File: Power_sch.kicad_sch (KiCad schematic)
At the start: 13 parts, among them J1 USB4105-GF-A, J2 USB4105-GF-A, U1 LD39200PU33R, U2 TPD2EUSB30ADRTR

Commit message: Updata the USB Hub Sheet
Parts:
- R1: footprint (none) -> Resistor_SMD:R_0402_1005Metric
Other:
- note removed: "POWER_ESD"
- moved on the sheet: D3, D4, F1, J1, J2, R1, R2, R3, R4, U1, U2

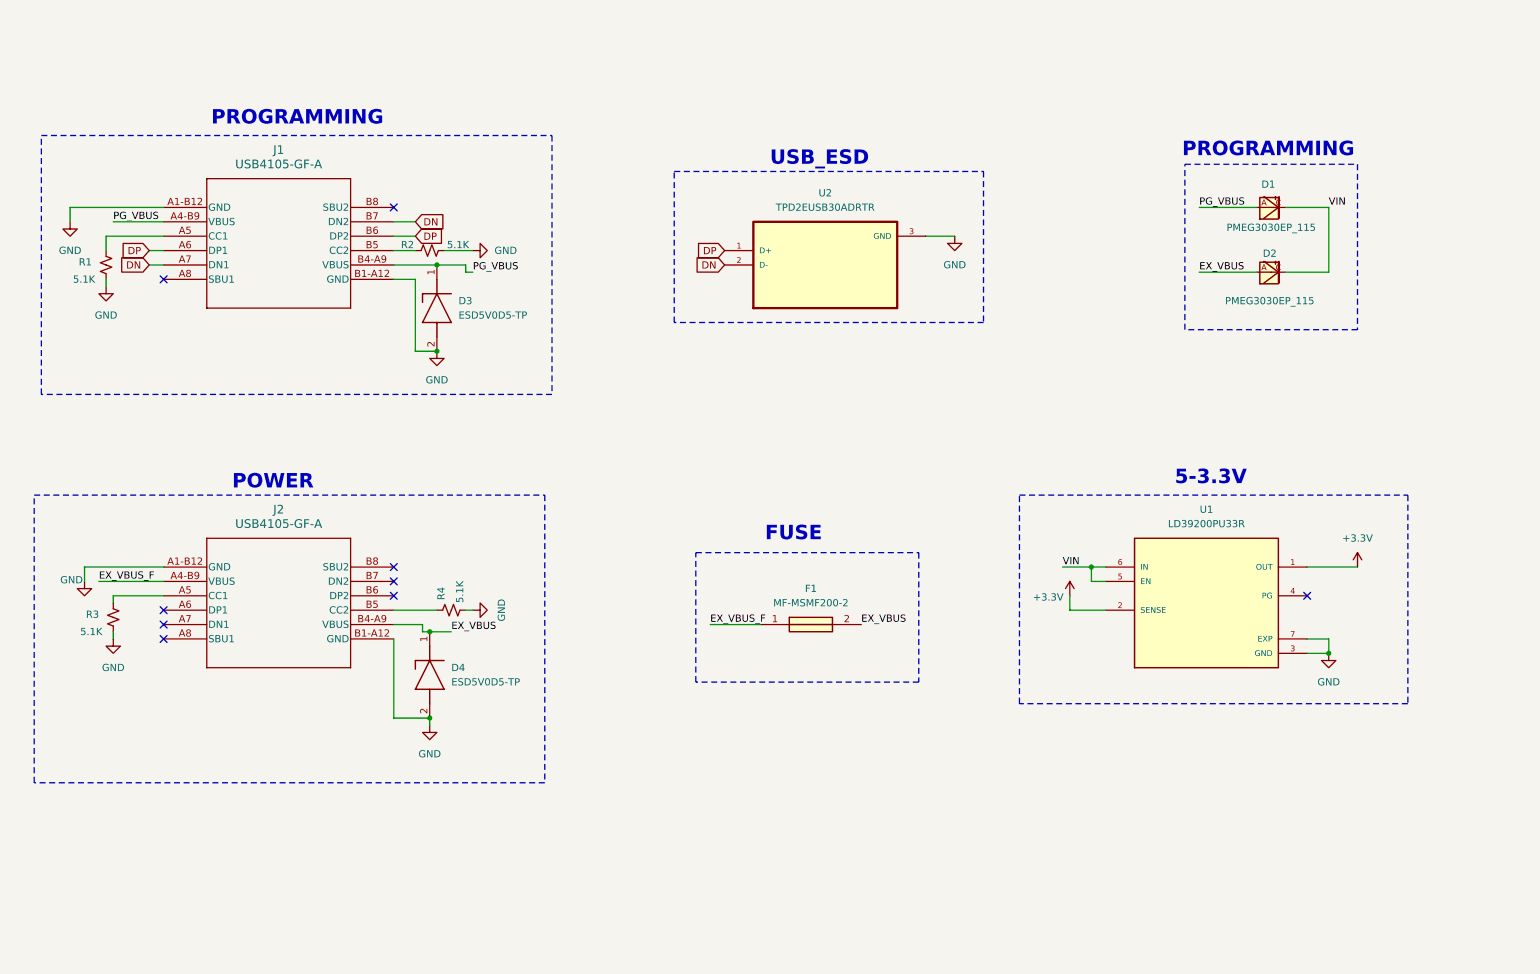
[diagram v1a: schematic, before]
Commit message: update the power sheet
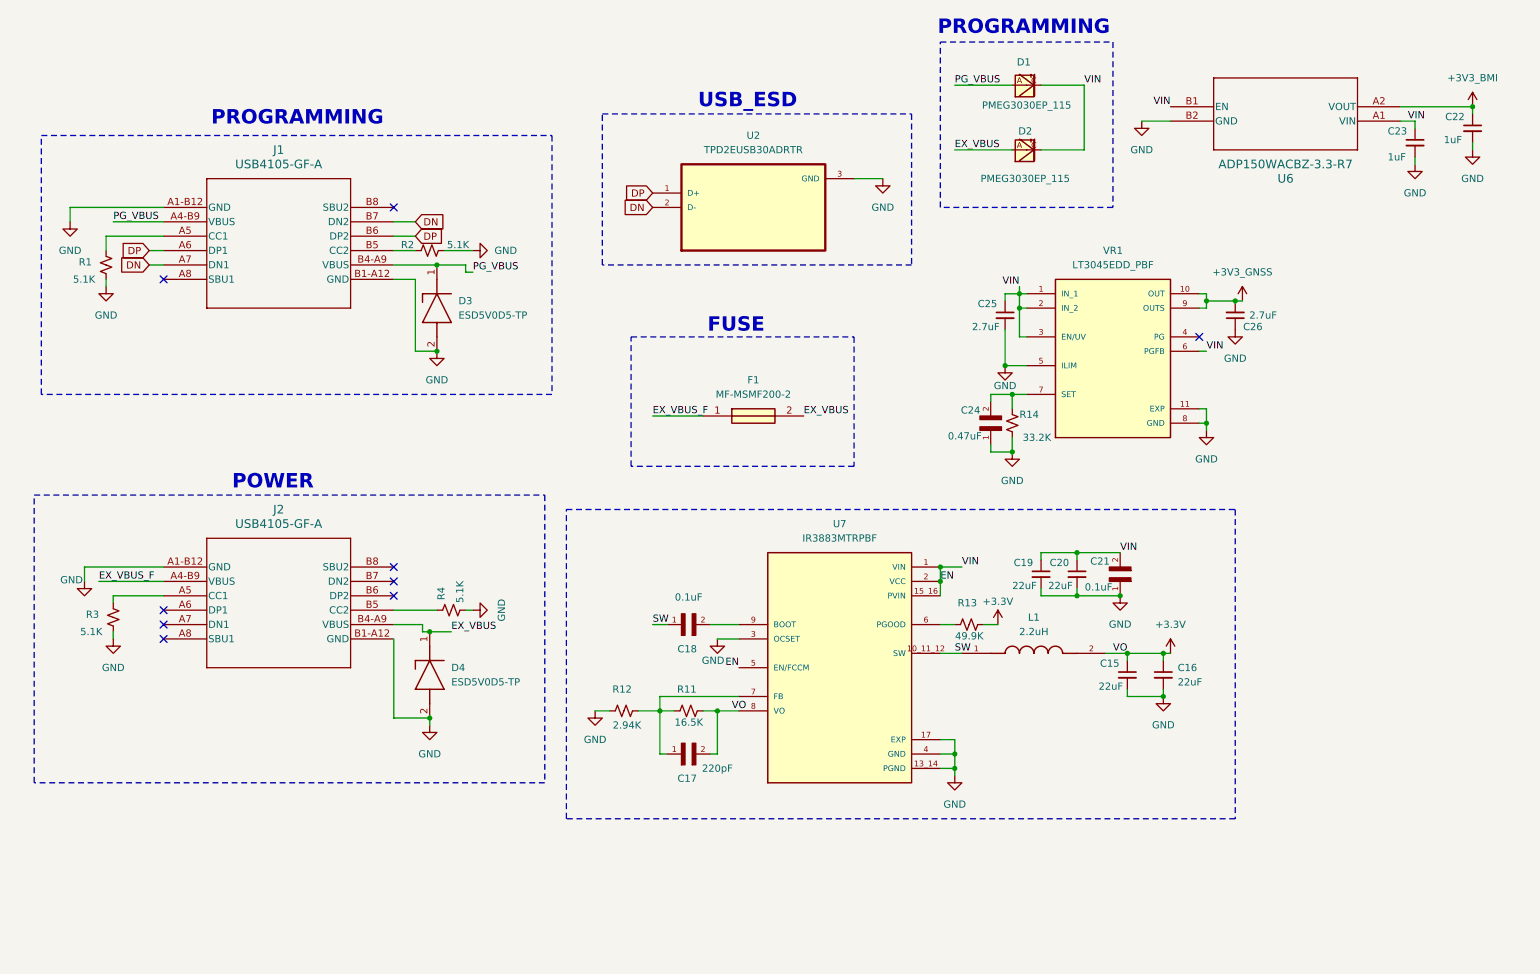
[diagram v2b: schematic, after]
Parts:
- removed U1: LD39200PU33R, LD39200PU33R:SON95P300X300X100-7N, symbol LD39200PU33R:LD39200PU33R
- added C15, C16, C19, C20: 22uF, Capacitor_SMD:C_0805_2012Metric, symbol Device:C_Small
- added C17: 220pF, C0402C104K4RAC:CAPC1005X55N, symbol C0402C104K4RAC:C0402C104K4RAC
- added C18, C21: 0.1uF, C0402C104K4RAC:CAPC1005X55N, symbol C0402C104K4RAC:C0402C104K4RAC
- added C22, C23: 1uF, Capacitor_SMD:C_0805_2012Metric, symbol Device:C_Small
- added C24: 0.47uF, C0402C104K4RAC:CAPC1005X55N, symbol C0402C104K4RAC:C0402C104K4RAC
- added C25, C26: 2.7uF, Capacitor_SMD:C_0805_2012Metric, symbol Device:C_Small
- added L1: 2.2uH, ASPIAIG-F5030-2R2M-T:IND_ASPIAIG-F5030-2R2M-T, symbol ASPIAIG-F5030-2R2M-T:ASPIAIG-F5030-2R2M-T
- added R11: 16.5K, Resistor_SMD:R_0402_1005Metric, symbol Device:R_Small_US
- added R12: 2.94K, Resistor_SMD:R_0402_1005Metric, symbol Device:R_Small_US
- added R13: 49.9K, Resistor_SMD:R_0402_1005Metric, symbol Device:R_Small_US
- added R14: 33.2K, Resistor_SMD:R_0402_1005Metric, symbol Device:R_Small_US
- added U6: ADP150WACBZ-3.3-R7, Module:CB-4-3_ADI, symbol 2026-08-11_06-36-10:ADP150WACBZ-3.3-R7
- added U7: IR3883MTRPBF, Module:VREG_IR3883MTRPBF, symbol IR3883MTRPBF:IR3883MTRPBF
- added VR1: LT3045EDD_PBF, Module:SON50P300X300X80-11N, symbol LT3045EDD_PBF:LT3045EDD_PBF
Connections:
- net +3.3V: now also C15.1, C16.1, C17.2, L1.2, R11.1, R13.1, U7.8 (VO)
- net GND: now also C15.2, C16.2, C19.2, C20.2, C21.1, C22.2, C23.2, C24.1, C25.2, C26.1, R12.2, R14.2, U6.B2 (GND), U7.13_14 (PGND), U7.17 (EXP), U7.3 (OCSET), U7.4 (GND), VR1.11 (EXP), VR1.5 (ILIM), VR1.8 (GND)
- net VIN renamed EN
- net EN: now also C19.1, C20.1, C21.2, C23.1, C25.1, U6.A1 (VIN), U6.B1 (EN), U7.1 (VIN), U7.15_16 (PVIN), U7.2 (VCC), U7.5 (EN/FCCM), VR1.1 (IN_1), VR1.2 (IN_2), VR1.3 (EN/UV), VR1.6 (PGFB)
- new net: C24.2, R14.1, VR1.7 (SET)
- new net: R13.2, U7.6 (PGOOD)
- new net: C17.1, R11.2, R12.1, U7.7 (FB)
- new net: C18.2, U7.9 (BOOT)
- new net +3V3_BMI: C22.1, U6.A2 (VOUT)
- new net +3V3_GNSS: C26.2, VR1.10 (OUT), VR1.9 (OUTS)
- new net SW: C18.1, L1.1, U7.10_11_12 (SW)
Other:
- note removed: "5-3.3V"
- moved on the sheet: D1, D2, F1, U2

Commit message: Add the STM
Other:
- note added: "3V3_BMI"
- note added: "3V3_GNSS"
- note added: "Buck_Converter"
- note added: "Power_Supply_'OR'ing"
- moved on the sheet: C15, C16, C17, C18, C19, C20, C21, C22, C23, C24, C25, C26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

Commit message: arrange the Sheets
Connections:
- net EN renamed VIN

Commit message: verification
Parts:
- added TP2, TP3, TP4, TP5: TestPoint, TestPoint:TestPoint_Pad_D2.0mm, symbol Connector:TestPoint
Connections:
- net +3.3V: now also TP5.1
- net +3V3_BMI: now also TP4.1
- net GND: now also TP2.1
- net VIN: now also TP3.1

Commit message: new
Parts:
- added F2: MF-MSMF200-2, FUSC4632X85N, symbol MF-MSMF200-2:MF-MSMF200-2
- added TP12: TestPoint, TestPoint:TestPoint_Pad_D2.0mm, symbol Connector:TestPoint
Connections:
- net +3V3_GNSS: now also TP12.1
- net EX_VBUS: now also J2.A4-B9 (VBUS), F2.2; no longer D4.1 (K), F1.2, J2.B4-A9 (VBUS)
- net PG_VBUS: now also F1.2; no longer D3.1 (K), J1.B4-A9 (VBUS)
- net EX_VBUS_F: no longer names the net of F1.1
- net EX_VBUS_F: now also D3.1 (K), J1.B4-A9 (VBUS); no longer J2.A4-B9 (VBUS)
- new net: D4.1 (K), F2.1, J2.B4-A9 (VBUS)
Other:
- note removed: "FUSE"
- moved on the sheet: C19, C20, C21, C22, C23, D3, D4, F1, J1, J2, R1, R2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
